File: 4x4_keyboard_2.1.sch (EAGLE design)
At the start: 77 parts, among them U2 AMS1117-5.0

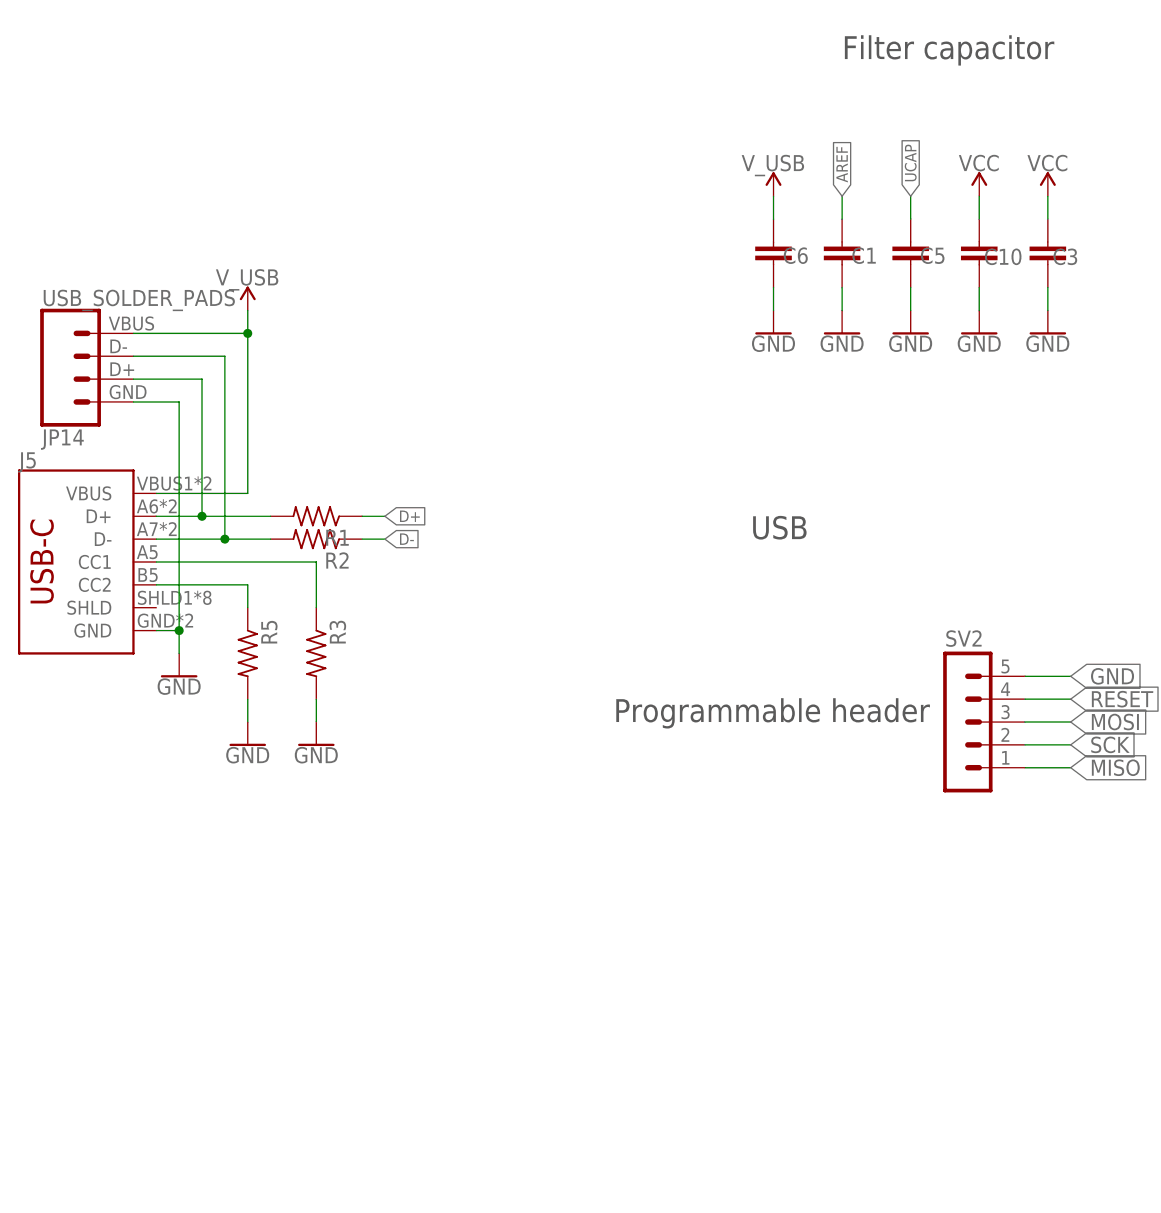
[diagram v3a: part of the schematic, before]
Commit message: change location of cherry switches
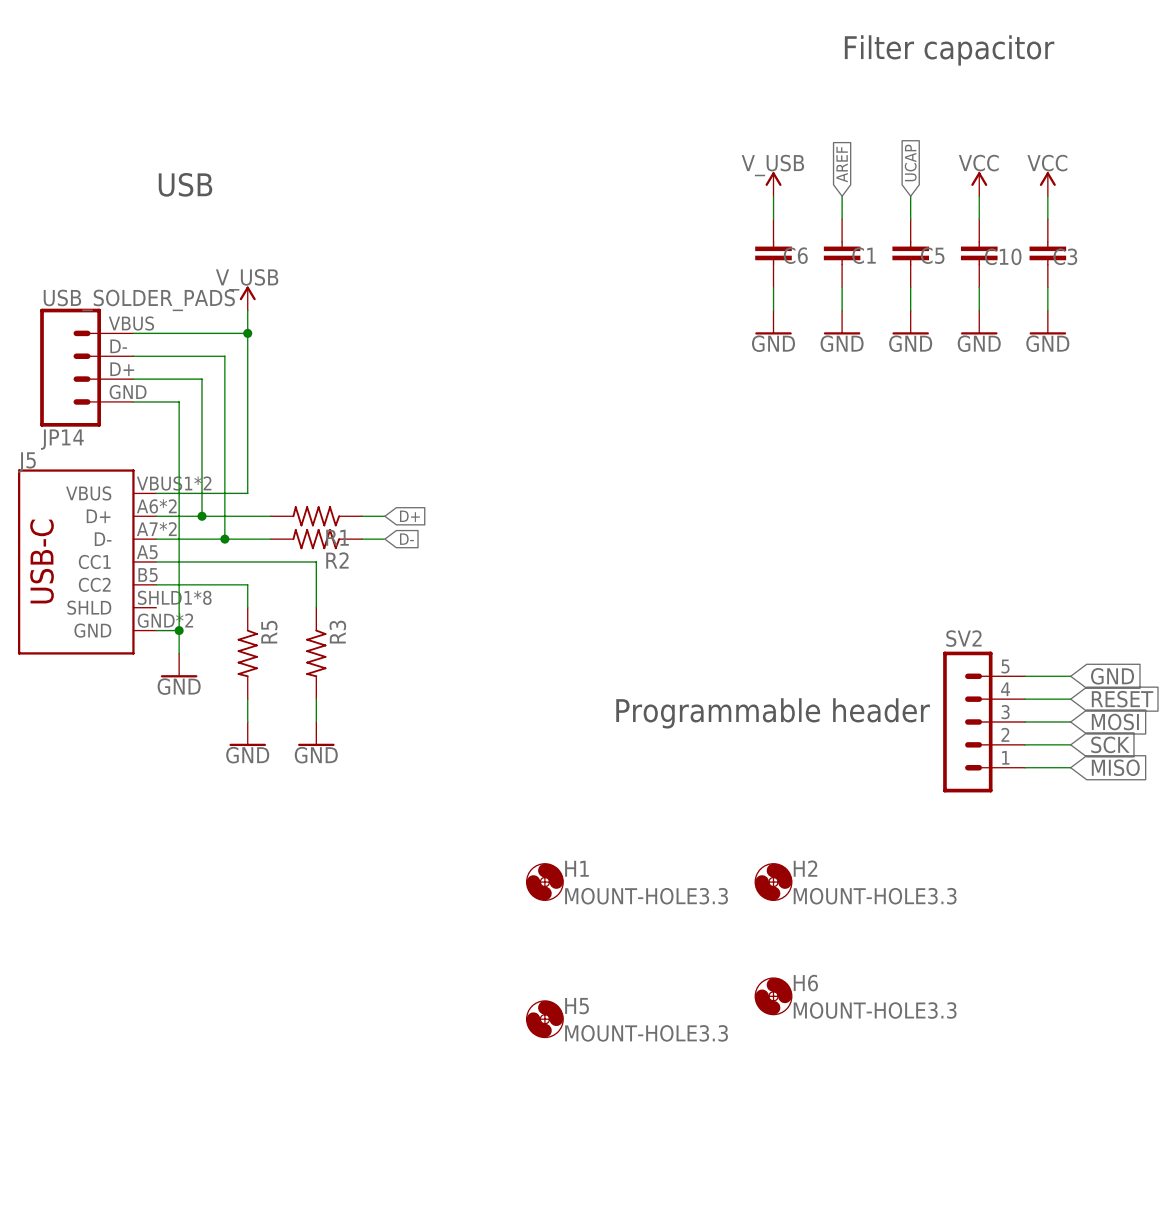
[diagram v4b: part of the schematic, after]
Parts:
- added H1, H2, H5, H6: MOUNT-HOLE3.3, holes:MOUNT-HOLE3.3
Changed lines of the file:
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@@
 <?xml version="1.0" encoding="utf-8"?>
 <!DOCTYPE eagle SYSTEM "eagle.dtd">
-<eagle version="9.6.2">
+<eagle version="6.4">
 <drawing>
 <settings>
 <setting alwaysvectorfont="no"/>
-<setting keepoldvectorfont="yes"/>
 <setting verticaltext="up"/>
 </settings>
@@
 <part name="R3" library="audio amplifier example" deviceset="R-US_" device="R0603" value="5.1k"/>
 <part name="R5" library="audio amplifier example" deviceset="R-US_" device="R0603" value="5.1k"/>
+<part name="H1" library="holes" deviceset="MOUNT-HOLE" device="3.3"/>
+<part name="H2" library="holes" deviceset="MOUNT-HOLE" device="3.3"/>
+<part name="H6" library="holes" deviceset="MOUNT-HOLE" device="3.3"/>
+<part name="H5" library="holes" deviceset="MOUNT-HOLE" device="3.3"/>
 </parts>
 <sheets>
@@
 <text x="-17.78" y="373.38" size="2.54" layer="97">Power supply</text>
 <text x="-96.52" y="347.98" size="2.54" layer="97">Filter capacitor</text>
-<text x="-106.68" y="294.64" size="2.54" layer="97">USB</text>
+<text x="-172.72" y="332.74" size="2.54" layer="97">USB</text>
 <text x="-121.92" y="274.32" size="2.54" layer="97">Programmable header</text>
 <text x="-17.78" y="200.66" size="2.54" layer="97">Encoder</text>
@@
 <attribute name="NAME" x="-161.0614" y="285.75" size="1.778" layer="95" rot="R270"/>
 </instance>
+<instance part="H1" gate="G$1" x="-129.54" y="256.54" smashed="yes">
+<attribute name="NAME" x="-127.508" y="257.1242" size="1.778" layer="95"/>
+<attribute name="VALUE" x="-127.508" y="254.0762" size="1.778" layer="96"/>
+</instance>
+<instance part="H2" gate="G$1" x="-104.14" y="256.54" smashed="yes">
+<attribute name="NAME" x="-102.108" y="257.1242" size="1.778" layer="95"/>
+<attribute name="VALUE" x="-102.108" y="254.0762" size="1.778" layer="96"/>
+</instance>
+<instance part="H6" gate="G$1" x="-104.14" y="243.84" smashed="yes">
+<attribute name="NAME" x="-102.108" y="244.4242" size="1.778" layer="95"/>
+<attribute name="VALUE" x="-102.108" y="241.3762" size="1.778" layer="96"/>
+</instance>
+<instance part="H5" gate="G$1" x="-129.54" y="241.3" smashed="yes">
+<attribute name="NAME" x="-127.508" y="241.8842" size="1.778" layer="95"/>
+<attribute name="VALUE" x="-127.508" y="238.8362" size="1.778" layer="96"/>
+</instance>
 </instances>

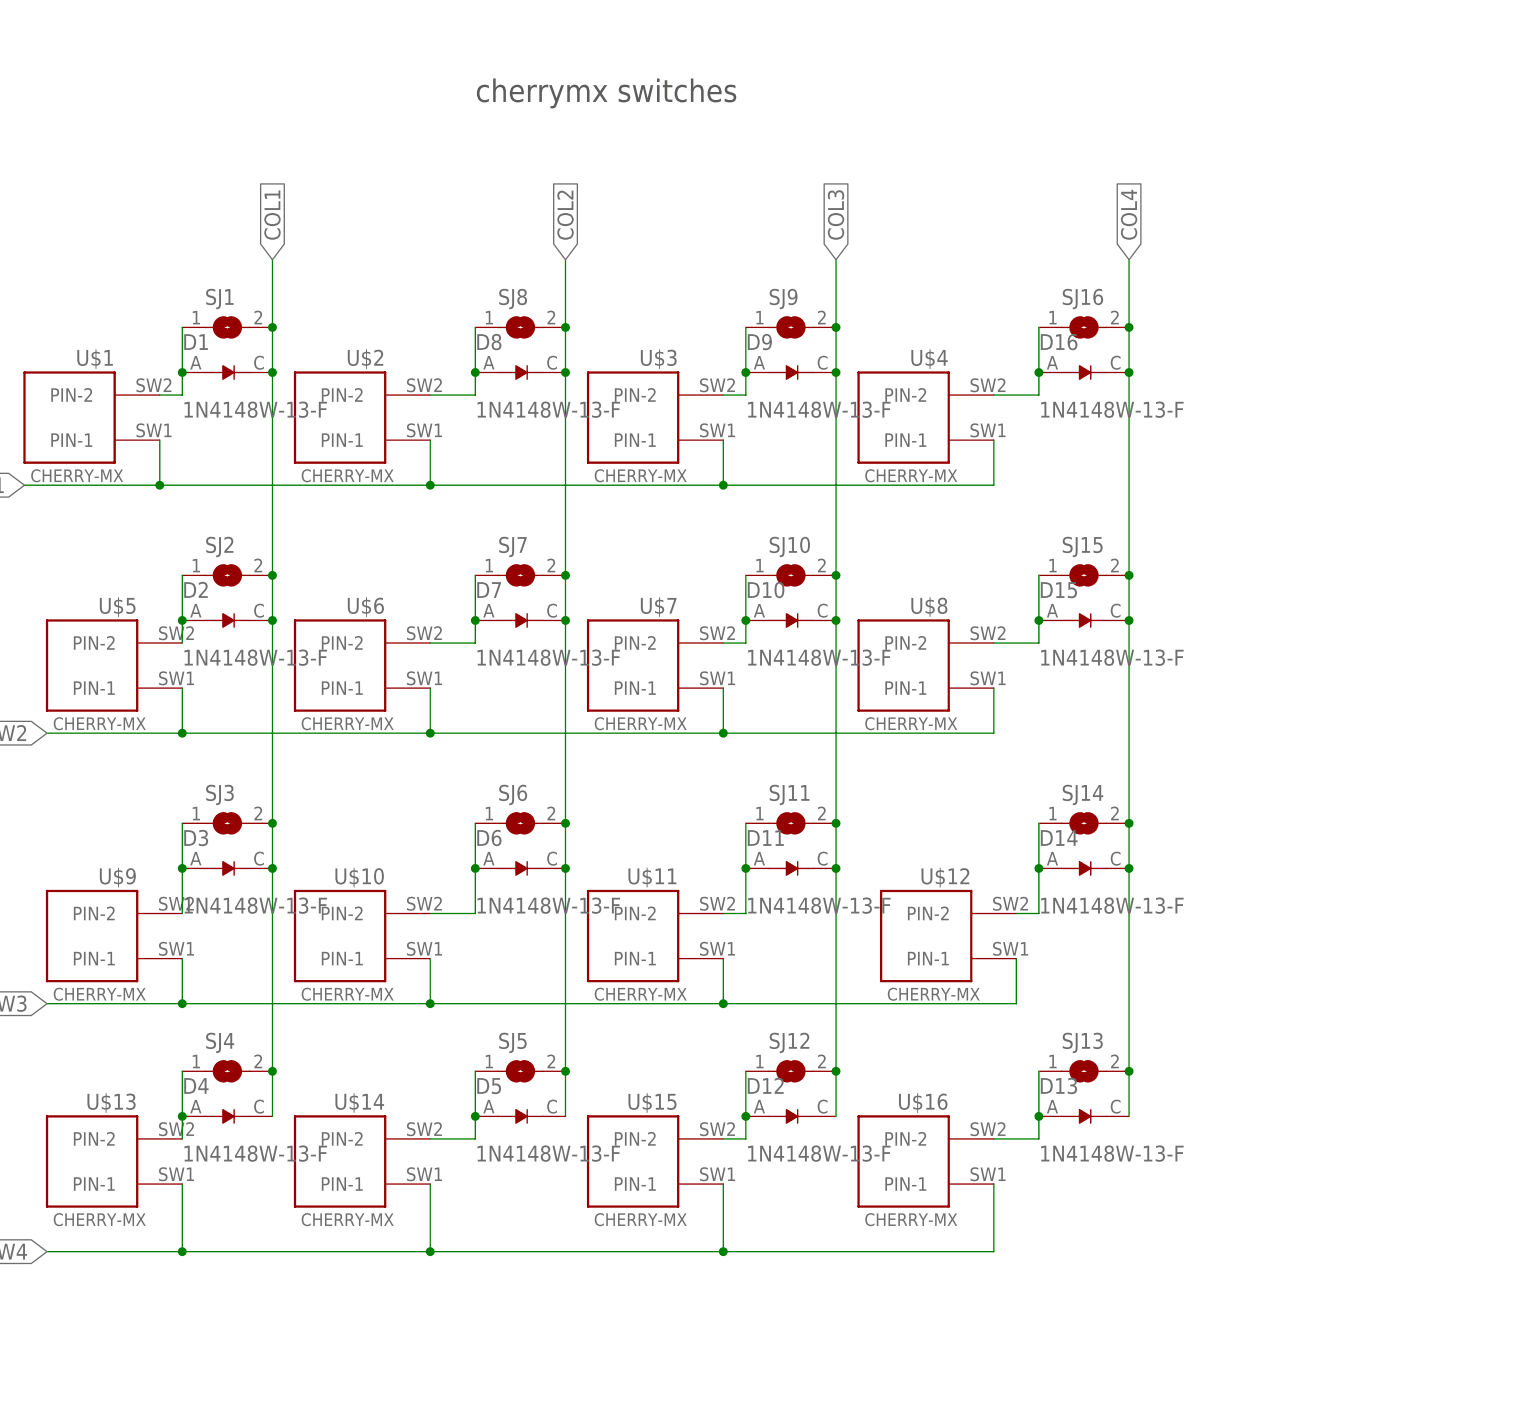
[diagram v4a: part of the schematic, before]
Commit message: routing cherry mx switch and correct the position of diode and rotary encoder
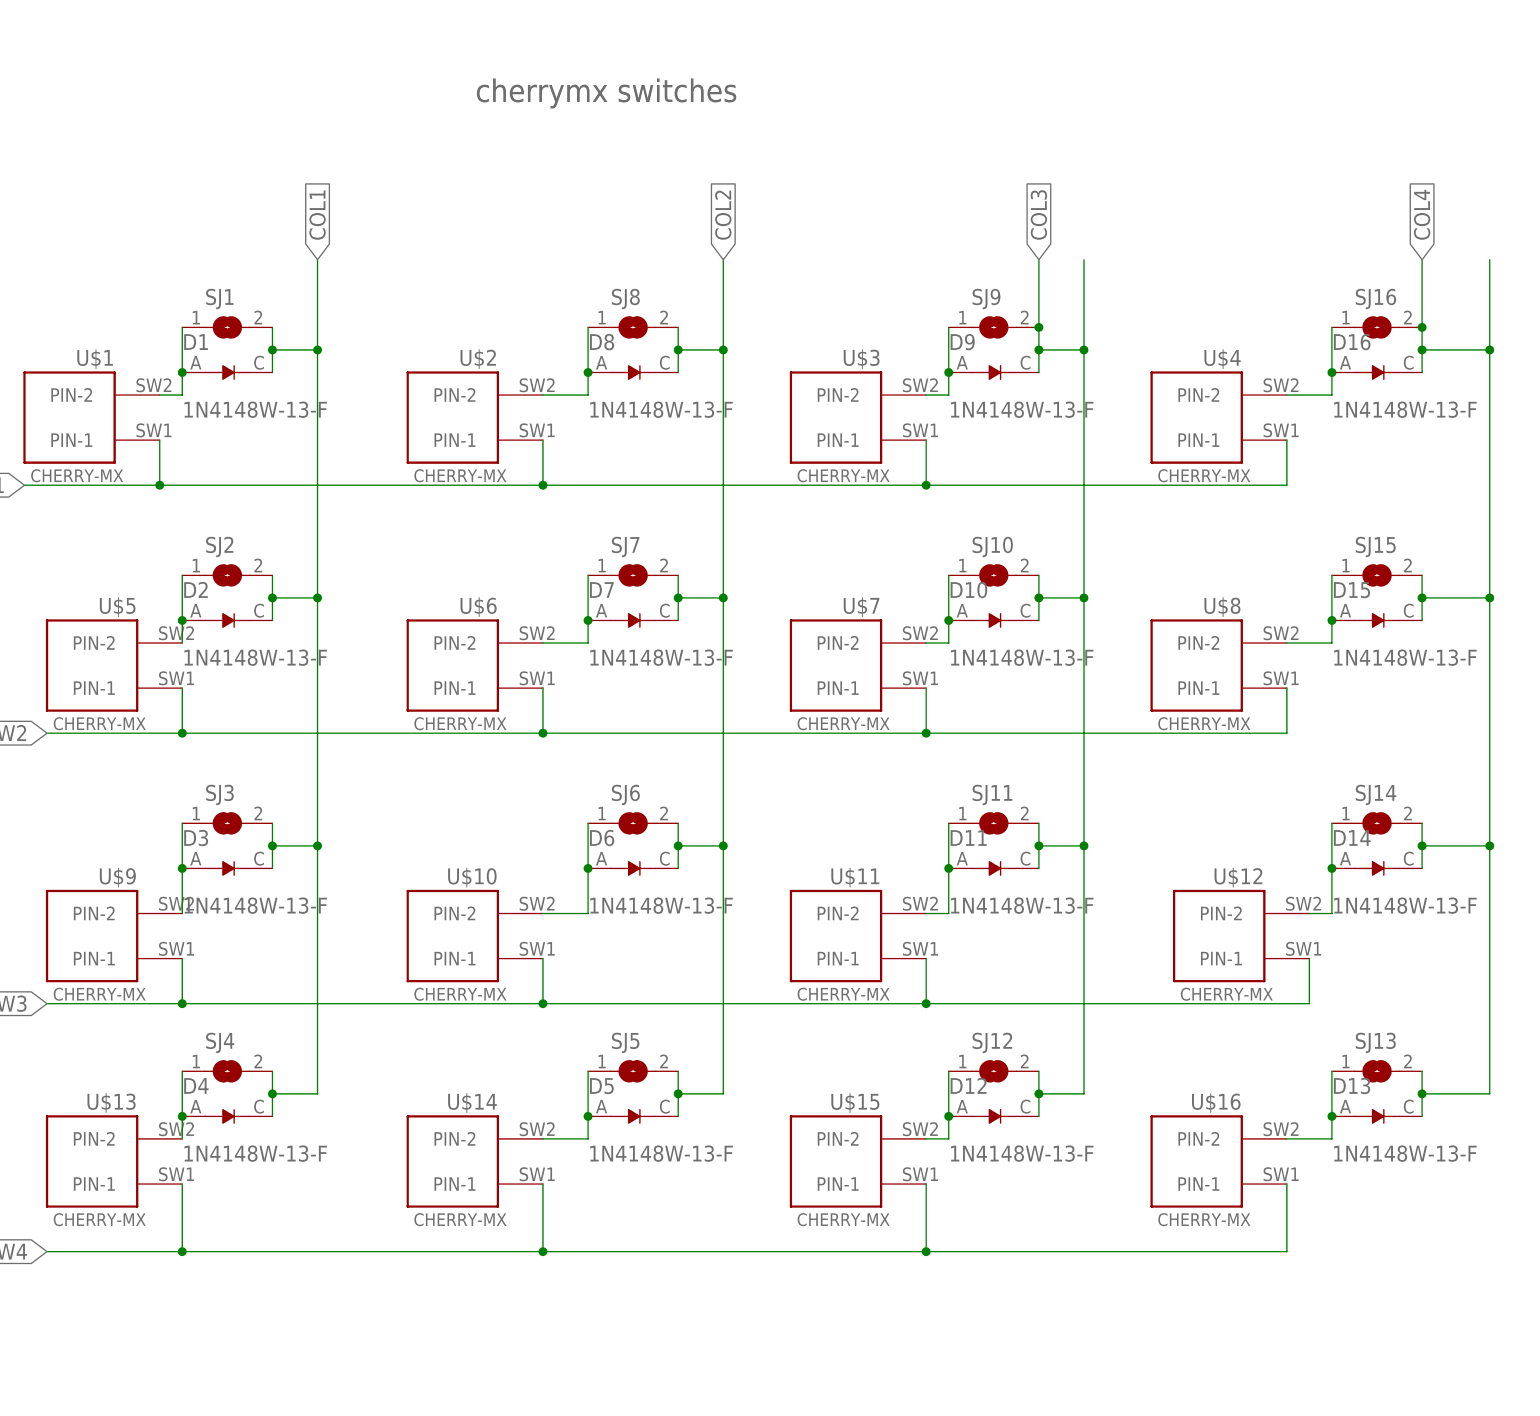
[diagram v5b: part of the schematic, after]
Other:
- moved on the sheet: D10, D11, D12, D13, D14, D15, D16, D5, D6, D7, D8, D9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

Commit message: Routing complete
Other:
- moved on the sheet: H5, H6
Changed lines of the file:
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@@
 <attribute name="VALUE" x="-102.108" y="254.0762" size="1.778" layer="96"/>
 </instance>
-<instance part="H6" gate="G$1" x="-104.14" y="243.84" smashed="yes">
-<attribute name="NAME" x="-102.108" y="244.4242" size="1.778" layer="95"/>
-<attribute name="VALUE" x="-102.108" y="241.3762" size="1.778" layer="96"/>
+<instance part="H6" gate="G$1" x="-104.14" y="248.92" smashed="yes">
+<attribute name="NAME" x="-102.108" y="249.5042" size="1.778" layer="95"/>
+<attribute name="VALUE" x="-102.108" y="246.4562" size="1.778" layer="96"/>
 </instance>
-<instance part="H5" gate="G$1" x="-129.54" y="241.3" smashed="yes">
-<attribute name="NAME" x="-127.508" y="241.8842" size="1.778" layer="95"/>
-<attribute name="VALUE" x="-127.508" y="238.8362" size="1.778" layer="96"/>
+<instance part="H5" gate="G$1" x="-129.54" y="246.38" smashed="yes">
+<attribute name="NAME" x="-127.508" y="246.9642" size="1.778" layer="95"/>
+<attribute name="VALUE" x="-127.508" y="243.9162" size="1.778" layer="96"/>
 </instance>
 </instances>
@@
 <wire x1="218.44" y1="340.36" x2="218.44" y2="337.82" width="0.1524" layer="91"/>
 <wire x1="218.44" y1="337.82" x2="218.44" y2="335.28" width="0.1524" layer="91"/>
-<wire x1="218.44" y1="340.36" x2="218.44" y2="347.98" width="0.1524" layer="91"/>
-<junction x="218.44" y="340.36"/>
-<label x="218.44" y="347.98" size="1.778" layer="95" rot="R90" xref="yes"/>
+<label x="226.06" y="347.98" size="1.778" layer="95" rot="R90" xref="yes"/>
 <pinref part="SJ15" gate="1" pin="2"/>
 <pinref part="D15" gate="G$1" pin="K"/>
@@
 <wire x1="175.26" y1="340.36" x2="175.26" y2="337.82" width="0.1524" layer="91"/>
 <wire x1="175.26" y1="337.82" x2="175.26" y2="335.28" width="0.1524" layer="91"/>
-<wire x1="175.26" y1="340.36" x2="175.26" y2="347.98" width="0.1524" layer="91"/>
-<junction x="175.26" y="340.36"/>
-<label x="175.26" y="347.98" size="1.778" layer="95" rot="R90" xref="yes"/>
+<label x="180.34" y="347.98" size="1.778" layer="95" rot="R90" xref="yes"/>
 <pinref part="SJ10" gate="1" pin="2"/>
 <pinref part="D10" gate="G$1" pin="K"/>

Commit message: added log
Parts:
- renumbered J5 to USB_C
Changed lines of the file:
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@@
 <part name="SUPPLY2" library="SparkFun-PowerSymbols" deviceset="V_USB" device=""/>
 <part name="JP14" library="SparkFun-Connectors" deviceset="USB_SOLDER_PADS" device=""/>
-<part name="J5" library="USBC" deviceset="USB_C" device="5"/>
+<part name="USB_C" library="USBC" deviceset="USB_C" device="5"/>
 <part name="R1" library="audio amplifier example" deviceset="R-US_" device="R0603" value="5.1k"/>
 <part name="R2" library="audio amplifier example" deviceset="R-US_" device="R0603" value="5.1k"/>
@@
 <attribute name="NAME" x="-185.42" y="306.832" size="1.778" layer="95" font="vector" rot="MR180"/>
 </instance>
-<instance part="J5" gate="J1" x="-185.42" y="292.1" smashed="yes">
+<instance part="USB_C" gate="J1" x="-185.42" y="292.1" smashed="yes">
 <attribute name="VALUE" x="-187.96" y="279.654" size="1.778" layer="96" font="vector" rot="MR180" align="top-left"/>
 <attribute name="NAME" x="-187.96" y="302.514" size="1.778" layer="95" font="vector"/>
@@
 <wire x1="-170.18" y1="309.88" x2="-170.18" y2="284.48" width="0.1524" layer="91"/>
 <junction x="-170.18" y="284.48"/>
-<pinref part="J5" gate="J1" pin="GND"/>
+<pinref part="USB_C" gate="J1" pin="GND"/>
 </segment>
 <segment>
@@
 <wire x1="-175.26" y1="317.5" x2="-162.56" y2="317.5" width="0.1524" layer="91"/>
 <junction x="-162.56" y="317.5"/>
-<pinref part="J5" gate="J1" pin="VBUS"/>
+<pinref part="USB_C" gate="J1" pin="VBUS"/>
 </segment>
 </net>
@@
 <wire x1="-165.1" y1="314.96" x2="-165.1" y2="294.64" width="0.1524" layer="91"/>
 <junction x="-165.1" y="294.64"/>
-<pinref part="J5" gate="J1" pin="D-"/>
+<pinref part="USB_C" gate="J1" pin="D-"/>
 <pinref part="R2" gate="G$1" pin="2"/>
 </segment>
@@
 <wire x1="-167.64" y1="312.42" x2="-167.64" y2="297.18" width="0.1524" layer="91"/>
 <junction x="-167.64" y="297.18"/>
-<pinref part="J5" gate="J1" pin="D+"/>
+<pinref part="USB_C" gate="J1" pin="D+"/>
 <pinref part="R1" gate="G$1" pin="2"/>
 </segment>
@@
 <wire x1="-172.72" y1="292.1" x2="-154.94" y2="292.1" width="0.1524" layer="91"/>
 <wire x1="-154.94" y1="292.1" x2="-154.94" y2="287.02" width="0.1524" layer="91"/>
-<pinref part="J5" gate="J1" pin="CC1"/>
+<pinref part="USB_C" gate="J1" pin="CC1"/>
 <pinref part="R3" gate="G$1" pin="1"/>
 </segment>
@@
 <wire x1="-172.72" y1="289.56" x2="-162.56" y2="289.56" width="0.1524" layer="91"/>
 <wire x1="-162.56" y1="289.56" x2="-162.56" y2="287.02" width="0.1524" layer="91"/>
-<pinref part="J5" gate="J1" pin="CC2"/>
+<pinref part="USB_C" gate="J1" pin="CC2"/>
 <pinref part="R5" gate="G$1" pin="1"/>
 </segment>
